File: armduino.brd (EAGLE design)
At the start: 68.6 x 53.4 mm, 64 parts, among them IC1 7805DT, IC2 LM358D, IC3 LM1117-3.3V, Q1 FDN360P, Q2 5MHz, Q3 8MHz, U1 MKL26Z128VFM4, U2 MKE02Z64VLD4, X1 POWERSUPPLY_DC21MMX, X2 USB-B_TH

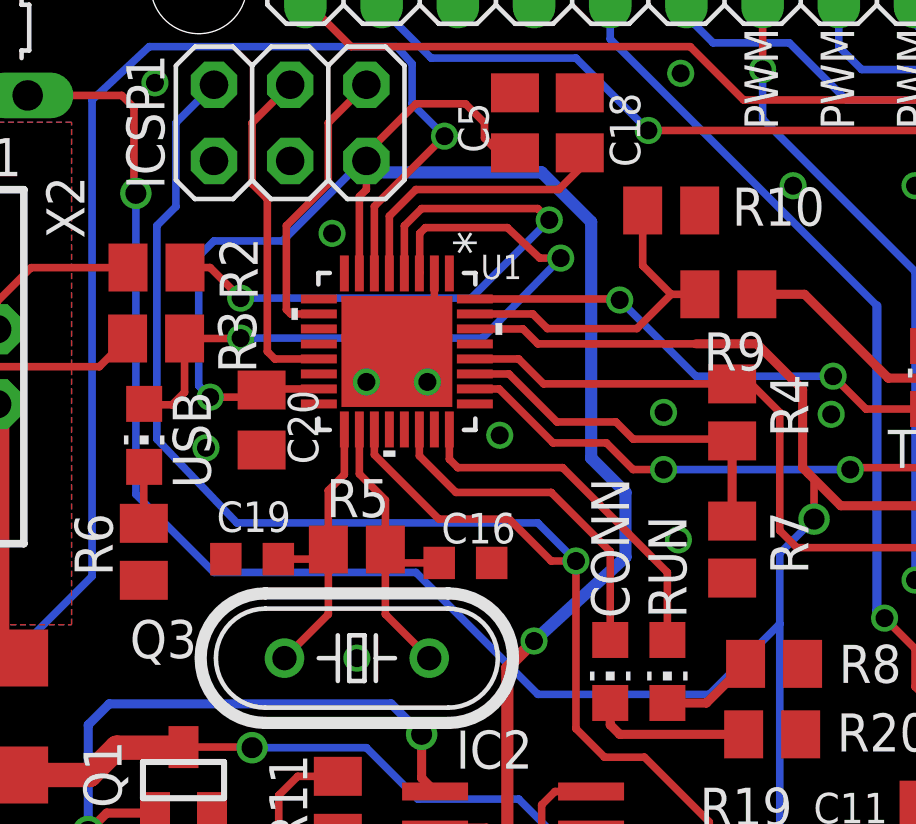
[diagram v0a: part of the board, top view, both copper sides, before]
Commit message: Update pad extension over QFN IC
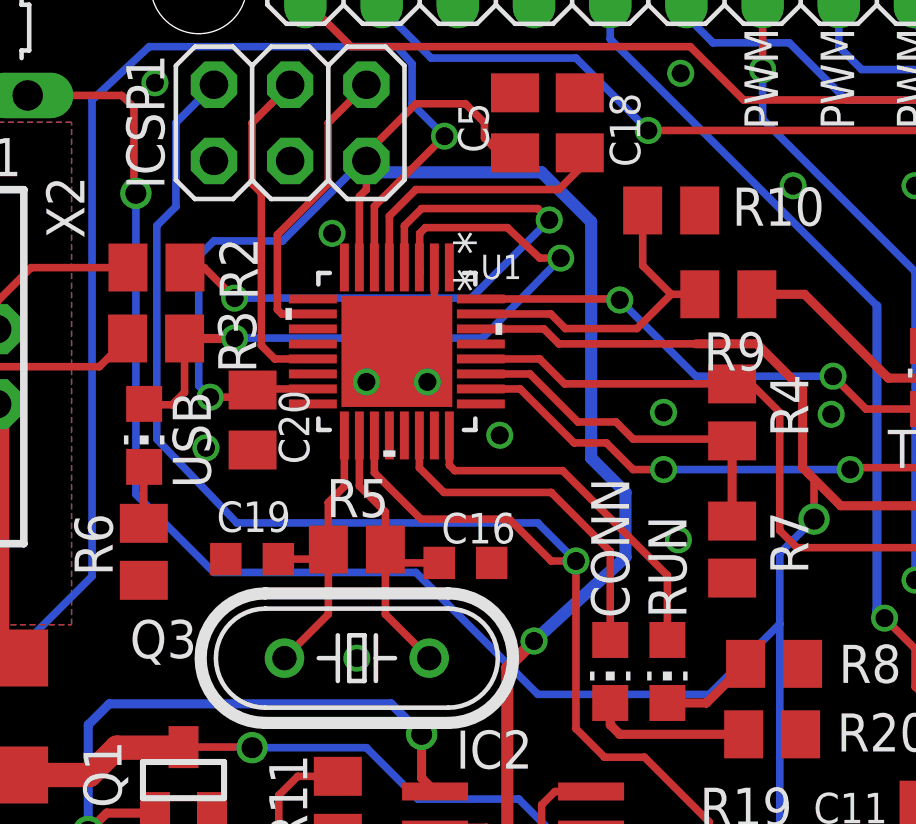
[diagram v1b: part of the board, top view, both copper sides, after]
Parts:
- moved C20 0.30 mm to (17.0, 36.3)
